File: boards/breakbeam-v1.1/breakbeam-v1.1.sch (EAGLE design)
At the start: 3 parts, among them X1 87438-02, X2 87438-02

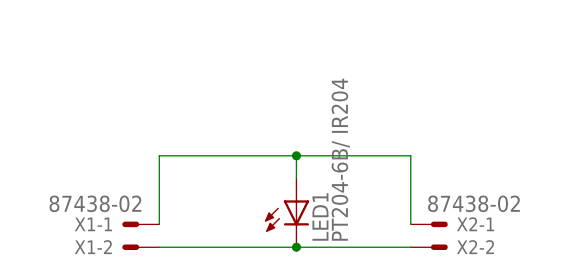
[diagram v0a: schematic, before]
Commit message: STLs of all boards on the robot are done
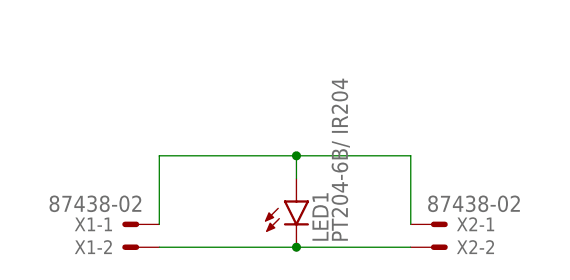
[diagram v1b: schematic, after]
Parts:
- LED1: device led:LED3MM -> RoboJackets-LEDs:LED-THROUGHHOLE3MM
- X1, X2: device con-molex:87438-02 -> RoboJackets-Connectors:87438-02
